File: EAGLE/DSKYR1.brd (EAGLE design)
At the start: 96.5 x 55.9 mm, 6 parts, among them IC1 74HC595N, IC2 74HC595N, IC3 74HC595N

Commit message: Update guide, finalize gerber files
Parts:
- SV1: device con-lstb:MA05-1 -> con-lsta:FE06
- moved SV1 2.54 mm to (7.62, 67.3), turned to 90 degrees
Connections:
- removed net N$5: IC1.10, IC2.10, IC3.10, SV1.3
- net GND: now also SV1.1
- net N$1: now also SV1.6; no longer SV1.5
- net N$4: now also SV1.5; no longer SV1.4
- net N$6: now also SV1.2; no longer SV1.1
- net N$8: now also SV1.3; no longer SV1.2
- net VCC: now also IC1.10, IC2.10, IC3.10, SV1.4
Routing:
- net N$5: track 102.0 -> 0.00 mm, vias 2 -> 0
- net GND: track 63.7 -> 105.1 mm
- net VCC: track 96.8 -> 134.8 mm, vias 6 -> 3
- net N$8: track 99.0 -> 134.6 mm, vias 0 -> 3
- net N$4: track 112.1 -> 93.2 mm, vias 3 -> 0
- net N$22: track 86.8 -> 99.8 mm, vias 3 -> 1
- net N$6: track 22.8 -> 34.1 mm
- net N$13: track 61.2 -> 50.6 mm, vias 0 -> 1
- net N$1: track 105.6 -> 95.3 mm
- net N$9: track 16.6 -> 22.5 mm, vias 0 -> 3
- net N$10: track 48.2 -> 44.1 mm
- net N$16: track 48.6 -> 51.4 mm, vias 1 -> 0
- net N$11: track 54.4 -> 52.0 mm
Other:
- board text added: "DATA"
- board text added: "G"
- board text added: "GND"
- board text added: "RCK"
- board text added: "SCK"
- board text added: "VCC"

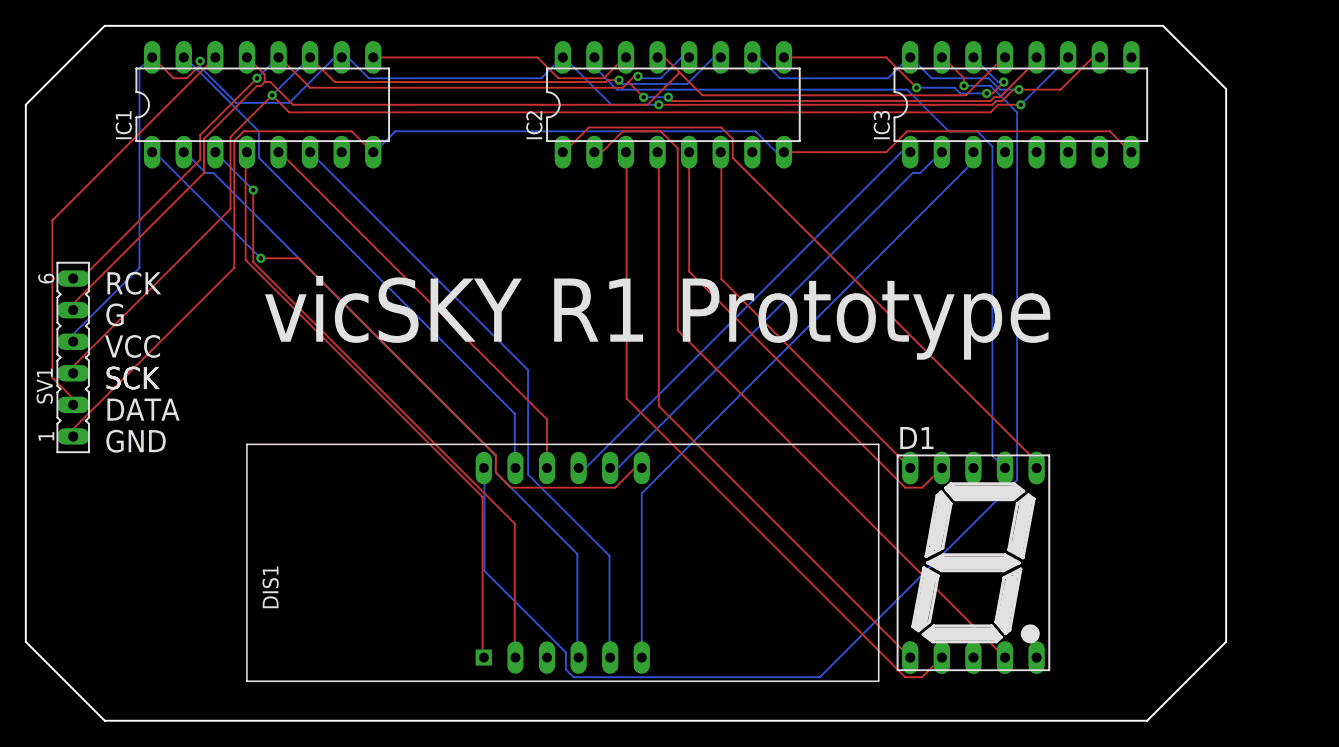
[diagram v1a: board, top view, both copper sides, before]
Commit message: Connect ground lines of R1D5
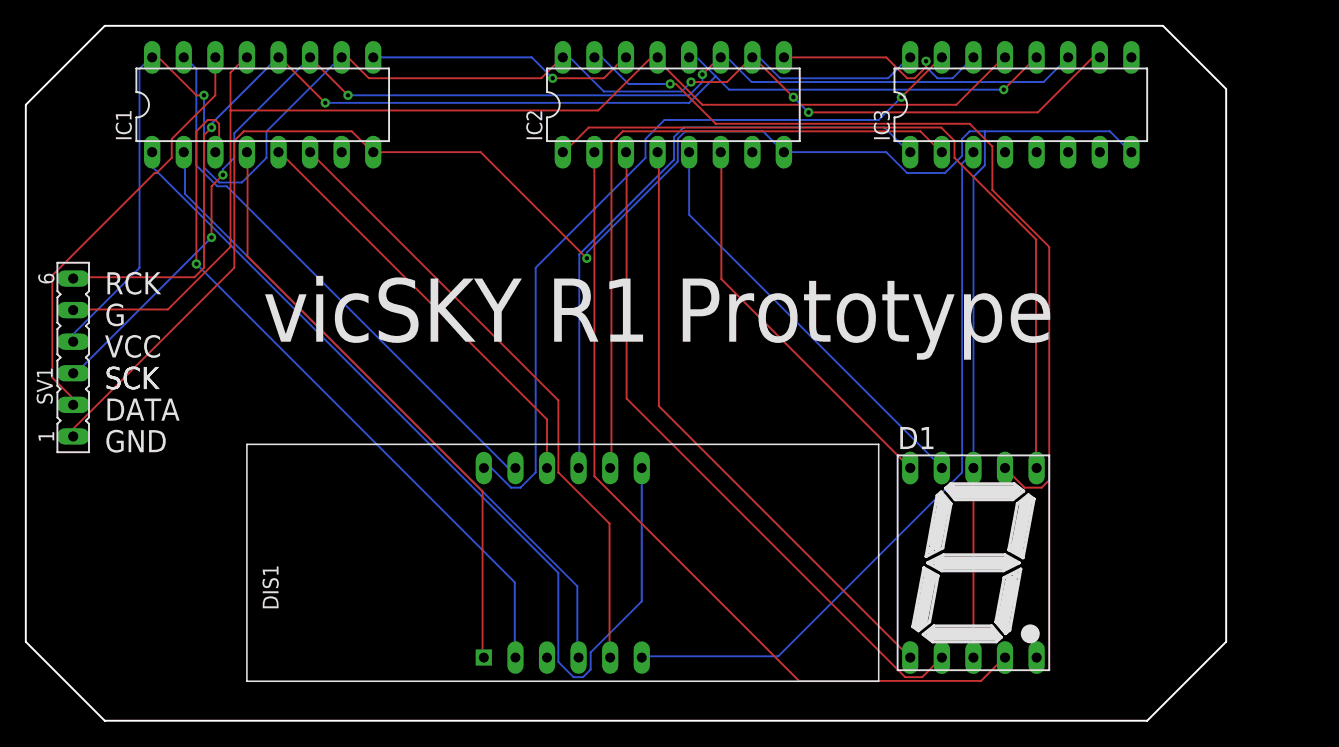
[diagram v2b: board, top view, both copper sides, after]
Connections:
- net GND: now also D1.3, D1.8
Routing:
- net GND: track 105.1 -> 158.4 mm, vias 0 -> 1
- net N$22: track 99.8 -> 62.3 mm
- net N$8: track 134.6 -> 99.0 mm, vias 3 -> 4
- net N$11: track 52.0 -> 75.8 mm, vias 1 -> 0
- net N$24: track 37.2 -> 53.8 mm
- net N$23: track 37.2 -> 49.9 mm
- net N$16: track 51.4 -> 61.8 mm
- net N$13: track 50.6 -> 57.7 mm
- net N$17: track 59.8 -> 66.7 mm
- net N$15: track 61.7 -> 68.1 mm, vias 0 -> 1
- net N$25: track 51.7 -> 58.1 mm
- net N$4: track 93.2 -> 98.0 mm
- net N$9: track 22.5 -> 18.3 mm, vias 3 -> 1
- net N$20: track 37.8 -> 33.8 mm
- net N$1: track 95.3 -> 98.0 mm, vias 4 -> 3
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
